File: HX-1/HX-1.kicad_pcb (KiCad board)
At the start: 2 copper layers, 45 x 90 mm, 91 parts, among them J1 USB_C_Receptacle_USB2.0_16P, J10 Conn_01x24, J12 USART, J2 Conn_01x02_Socket, J3 I2C, J4 SPI, J6 DEBUG, J8 UART, J9 Conn_01x24, SW1 BOOT0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

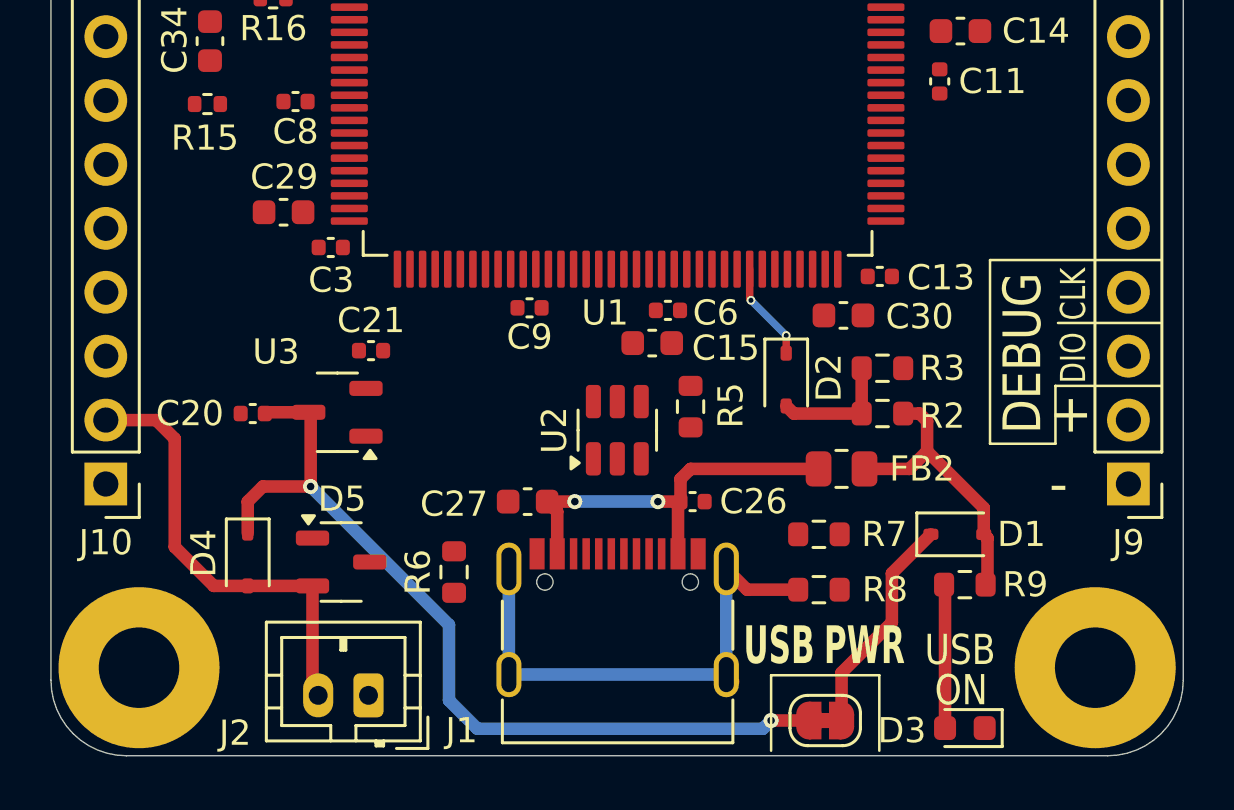
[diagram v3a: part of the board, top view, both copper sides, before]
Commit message: add silkscreen for batt in
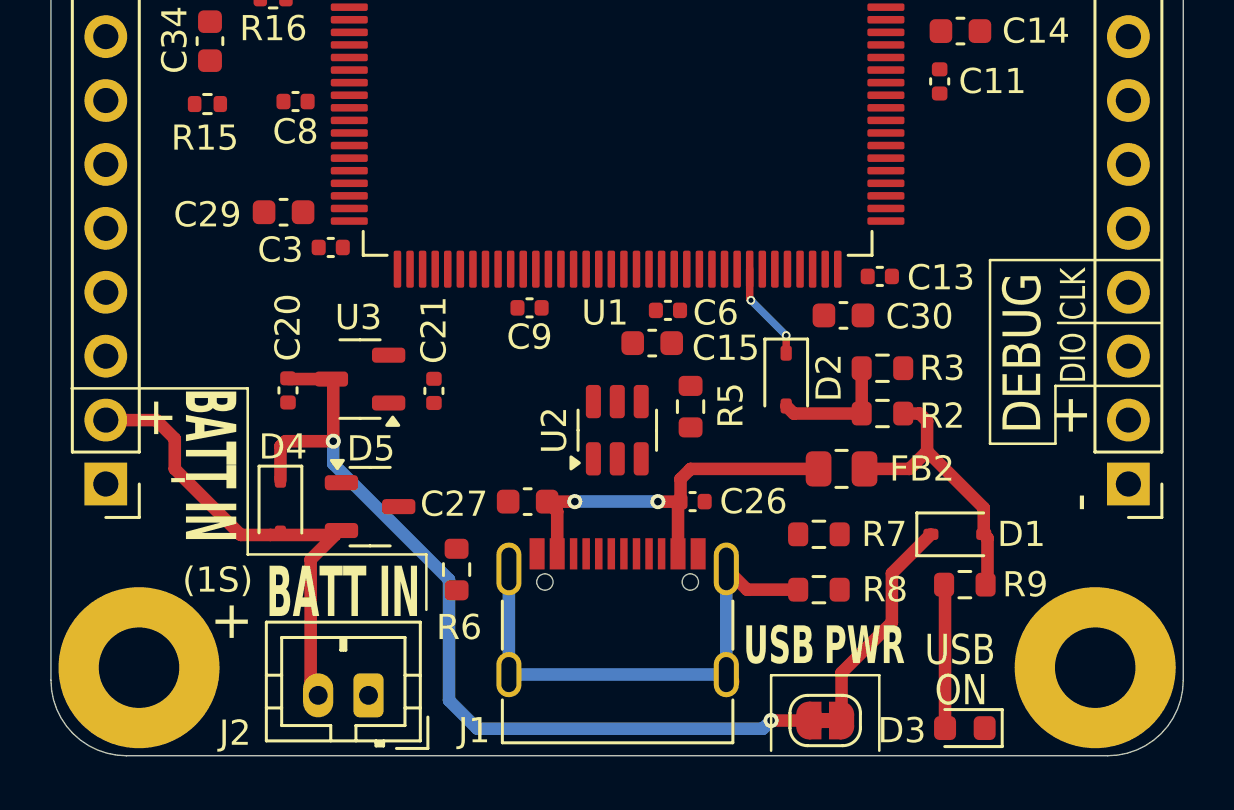
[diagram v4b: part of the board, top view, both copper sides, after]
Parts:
- moved C21 2.97 mm to (137.7, 132.5), turned to 90 degrees
- moved D5 2.48 mm to (135.2, 137.1)
- moved D4 2.47 mm to (131.6, 137.1)
- moved C20 1.68 mm to (131.9, 132.5), turned to 90 degrees
- moved U3 1.60 mm to (134.8, 132.0)
- moved R6 0.14 mm to (138.6, 139.6)
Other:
- board text added: "(1S)"
- board text added: "BATT IN"

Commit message: remove 3V3 out and replace with standard 3V3 in.
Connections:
- J9 pad 2: 3V3_OUT -> +3.3V

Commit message: remove GPIO 12 from MCU and firmware
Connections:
- U1 pad 29: /MCU/GPIO_12 -> unconnected-(U1-PC3_C-Pad29)
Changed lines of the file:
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@@
 	(net 141 "/MCU/GPIO_11")
 	(net 142 "/MCU/GPIO_5")
-	(net 143 "/MCU/GPIO_12")
+	(net 143 "unconnected-(U1-PC3_C-Pad29)")
 	(net 144 "/MCU/GPIO_3")
 	(net 145 "/MCU/GPIO_10")
@@
 			(layers "F.Cu" "F.Paste" "F.Mask")
 			(roundrect_rratio 0.25)
-			(net 143 "/MCU/GPIO_12")
+			(net 143 "unconnected-(U1-PC3_C-Pad29)")
 			(pinfunction "PC3_C")
-			(pintype "bidirectional")
+			(pintype "bidirectional+no_connect")
 		)
 		(pad "30" smd roundrect

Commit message: remove forgotten excess GPIO pins
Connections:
- U1 pad 74: /MCU/GPIO_15 -> unconnected-(U1-PB13-Pad74)
- U1 pad 77: /MCU/GPIO_15 -> unconnected-(U1-PD8-Pad77)
- U1 pad 78: /MCU/GPIO_16 -> unconnected-(U1-PD9-Pad78)
- U1 pad 79: /MCU/GPIO_17 -> unconnected-(U1-PD10-Pad79)
- U1 pad 80: /MCU/GPIO_18 -> unconnected-(U1-PD11-Pad80)
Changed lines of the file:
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@@
 	(net 50 "/MCU/SPI4_MISO")
 	(net 51 "/MCU/I2C_SCL")
-	(net 52 "/MCU/GPIO_16")
+	(net 52 "unconnected-(U1-PD9-Pad78)")
 	(net 53 "/MCU/USART2_TX")
 	(net 54 "unconnected-(U1-PG5-Pad90)")
 	(net 55 "/MCU/USART2_RX")
 	(net 56 "/MCU/TIM4_PWM_3")
-	(net 57 "/MCU/GPIO_15")
+	(net 57 "unconnected-(U1-PD8-Pad77)")
 	(net 58 "/MCU/DAC_1_OUT")
 	(net 59 "/MCU/UART8_TX")
@@
 	(net 65 "unconnected-(U1-PG8-Pad93)")
 	(net 66 "/MCU/TIM1_PWM_4")
-	(net 67 "/MCU/GPIO_17")
+	(net 67 "unconnected-(U1-PB13-Pad74)")
 	(net 68 "/MCU/TIM4_PWM_2")
 	(net 69 "/MCU/TIM23_PWM_1")
@@
 	(net 77 "/MCU/TIM12_PWM_2")
 	(net 78 "/MCU/SPI4_SCK")
-	(net 79 "/MCU/GPIO_18")
+	(net 79 "unconnected-(U1-PD11-Pad80)")
 	(net 80 "/MCU/FDCAN1_RX")
 	(net 81 "/MCU/TIM1_PWM_1-")
@@
 	(net 151 "/MCU/DEBUG_SWDIO")
 	(net 152 "/MCU/DEBUG_SWCLK")
+	(net 153 "unconnected-(U1-PD10-Pad79)")
 	(footprint "Capacitor_SMD:C_0402_1005Metric"
 		(layer "F.Cu")
@@
 			(layers "F.Cu" "F.Paste" "F.Mask")
 			(roundrect_rratio 0.25)
-			(net 57 "/MCU/GPIO_15")
+			(net 67 "unconnected-(U1-PB13-Pad74)")
 			(pinfunction "PB13")
-			(pintype "bidirectional")
+			(pintype "bidirectional+no_connect")
 		)
 		(pad "75" smd roundrect
@@
 			(layers "F.Cu" "F.Paste" "F.Mask")
 			(roundrect_rratio 0.25)
-			(net 57 "/MCU/GPIO_15")
+			(net 57 "unconnected-(U1-PD8-Pad77)")
 			(pinfunction "PD8")
-			(pintype "bidirectional")
+			(pintype "bidirectional+no_connect")
 		)
 		(pad "78" smd roundrect
@@
 			(layers "F.Cu" "F.Paste" "F.Mask")
 			(roundrect_rratio 0.25)
-			(net 52 "/MCU/GPIO_16")
+			(net 52 "unconnected-(U1-PD9-Pad78)")
 			(pinfunction "PD9")
-			(pintype "bidirectional")
+			(pintype "bidirectional+no_connect")
 		)
 		(pad "79" smd roundrect
@@
 			(layers "F.Cu" "F.Paste" "F.Mask")
 			(roundrect_rratio 0.25)
-			(net 67 "/MCU/GPIO_17")
+			(net 153 "unconnected-(U1-PD10-Pad79)")
 			(pinfunction "PD10")
-			(pintype "bidirectional")
+			(pintype "bidirectional+no_connect")
 		)
 		(pad "80" smd roundrect
@@
 			(layers "F.Cu" "F.Paste" "F.Mask")
 			(roundrect_rratio 0.25)
-			(net 79 "/MCU/GPIO_18")
+			(net 79 "unconnected-(U1-PD11-Pad80)")
 			(pinfunction "PD11")
-			(pintype "bidirectional")
+			(pintype "bidirectional+no_connect")
 		)
 		(pad "81" smd roundrect

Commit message: remove deprecated debug header, improve silkscreen pin designators
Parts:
- removed J6: DEBUG, Connector_PinHeader_2.54mm:PinHeader_1x04_P2.54mm_Vertical
- moved D7 5.11 mm to (157.8, 100.1)
- moved R26 5.11 mm to (157.7, 102.3)
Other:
- board text removed: "3.3V"
